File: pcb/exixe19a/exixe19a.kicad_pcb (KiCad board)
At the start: 2 copper layers, 39 parts, among them J1 Conn_01x07, J2 Conn_01x07, Q1 BF820W, Q10 BF820W, Q11 BF820W, Q3 MSB92W, Q4 BF820W, Q5 BF820W, Q6 BF820W, Q7 BF820W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

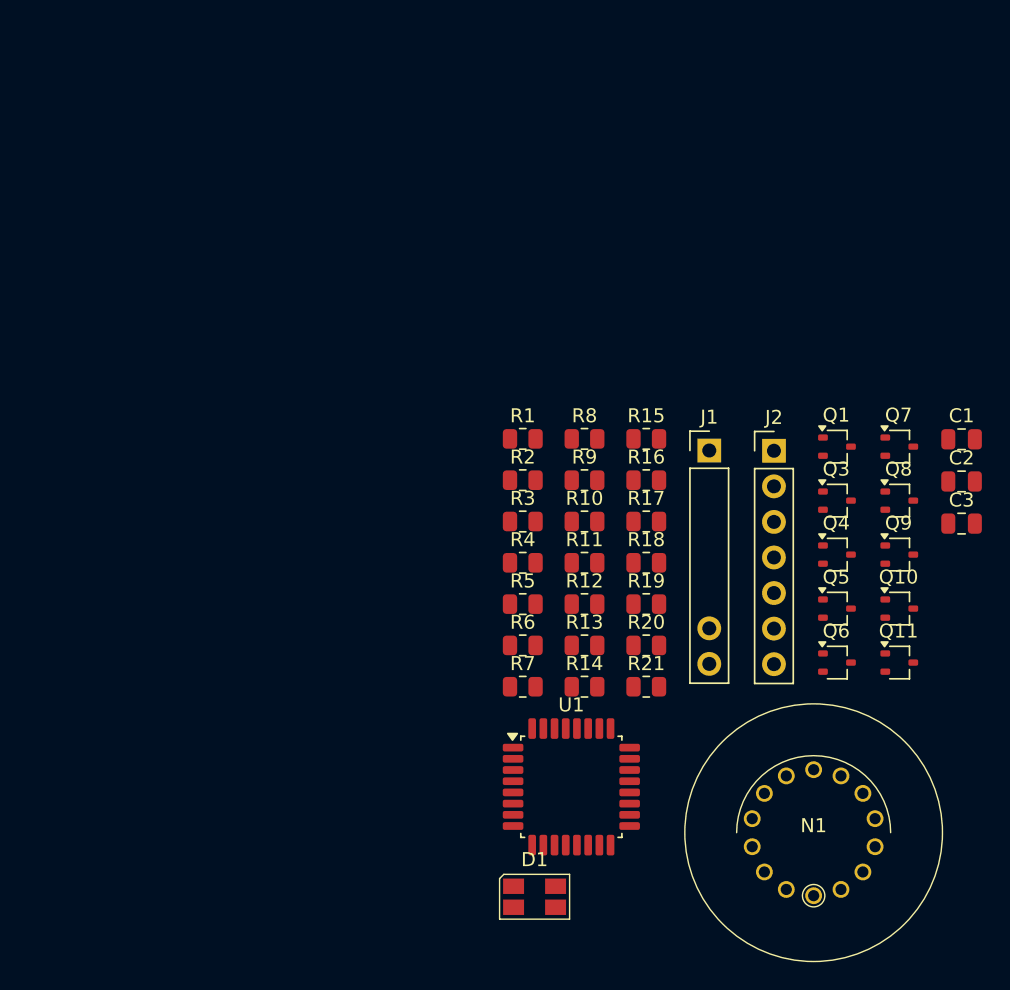
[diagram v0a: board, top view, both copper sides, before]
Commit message: pcb design for IN-19 tubes
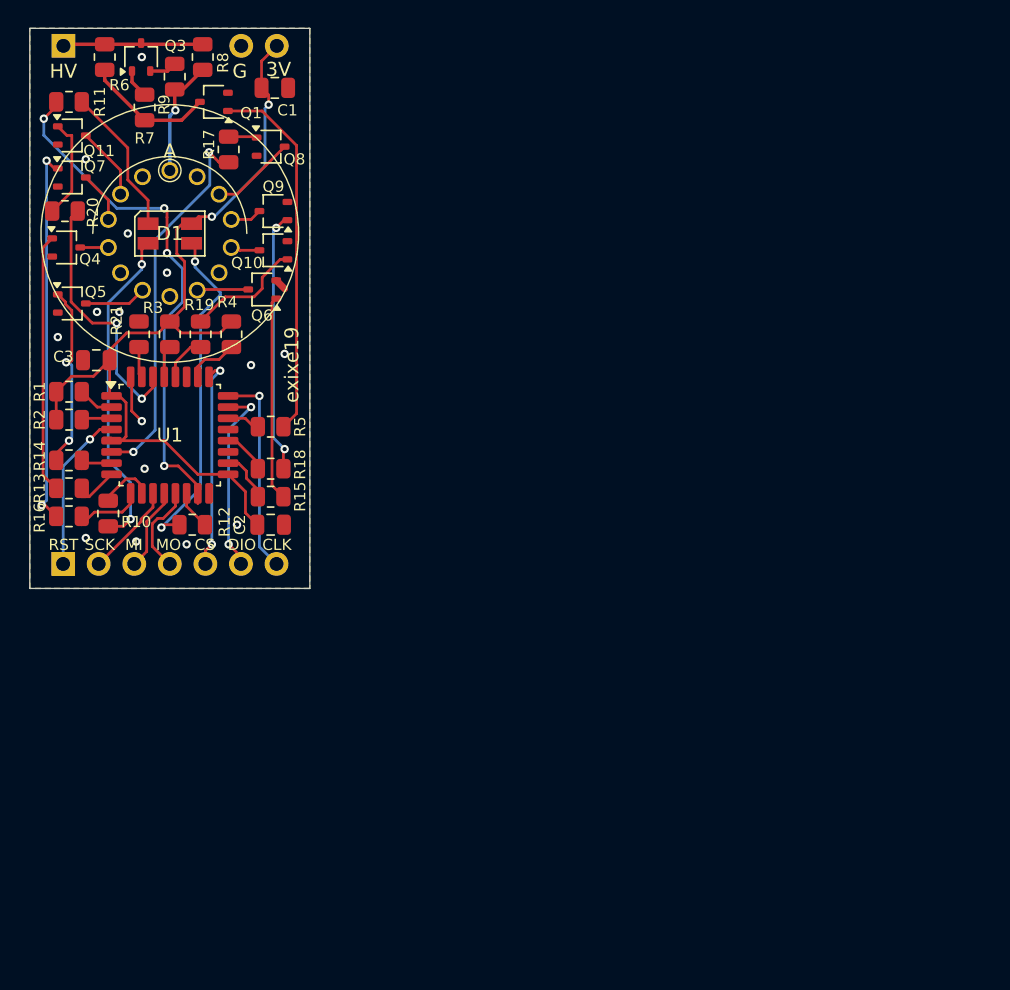
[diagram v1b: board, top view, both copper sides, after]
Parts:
- D1: footprint LED_SMD:LED_Avago_PLCC4_3.2x2.8mm_CW -> LED_SMD:LED_RGB_Wuerth-PLCC4_3.2x2.8mm_150141M173100
- moved Q11 70.1 mm to (33.0, 39.4)
- moved C3 62.9 mm to (34.8, 55.5), turned to 180 degrees
- moved N1 62.8 mm to (40.0, 46.4)
- moved Q7 62.1 mm to (33.0, 42.4)
- moved Q4 59.3 mm to (32.6, 47.4)
- moved Q3 58.9 mm to (38.0, 33.8), turned to 90 degrees
- moved Q5 58.8 mm to (33.0, 51.4)
- moved C1 55.1 mm to (47.5, 36.0)
- moved J1 54.4 mm to (32.4, 33.0), turned to 90 degrees
- moved D1 54.1 mm to (40.0, 46.4)
- moved R20 51.8 mm to (32.5, 44.8), turned to 180 degrees
- moved R6 51.5 mm to (35.4, 33.8), turned to -90 degrees
- moved Q8 51.5 mm to (47.2, 40.2)
- moved Q10 51.5 mm to (47.4, 47.6), turned to 180 degrees
- moved J2 51.4 mm to (32.4, 70.0), turned to 90 degrees
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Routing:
- net +3.3V: track 0.00 -> 64.9 mm, vias 0 -> 2
- net /PWM_RED: track 0.00 -> 37.3 mm, vias 0 -> 4
- net Net-(Q7-B): track 0.00 -> 27.1 mm, vias 0 -> 2
- net /STM_5: track 0.00 -> 26.9 mm, vias 0 -> 2
- net Net-(Q1-B): track 0.00 -> 26.4 mm
- net Net-(D1-BK): track 0.00 -> 24.3 mm, vias 0 -> 2
- net Net-(D1-GK): track 0.00 -> 23.4 mm, vias 0 -> 2
- net Net-(Q9-B): track 0.00 -> 18.7 mm, vias 0 -> 2
- net /STM_4: track 0.00 -> 18.6 mm, vias 0 -> 2
- net Net-(Q4-B): track 0.00 -> 18.5 mm
- net /SPI_CS: track 0.00 -> 15.7 mm, vias 0 -> 2
- net /SWD_CLK: track 0.00 -> 14.7 mm, vias 0 -> 1
- net Net-(Q6-B): track 0.00 -> 14.6 mm
- net /SWD_DIO: track 0.00 -> 13.9 mm, vias 0 -> 2
- net Net-(Q5-B): track 0.00 -> 12.9 mm, vias 0 -> 2
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- added copper zone on B.Cu, net GND
- added copper zone on F.Cu, net GND
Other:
- board outline added: 20 x 40 mm
- board text added: "3V"
- board text added: "A"
- board text added: "CLK"
- board text added: "CS"
- board text added: "DIO"
- board text added: "G"
- board text added: "HV"
- board text added: "MI"
- board text added: "MO"
- board text added: "RST"
- board text added: "SCK"
- board text added: "exixe19"
